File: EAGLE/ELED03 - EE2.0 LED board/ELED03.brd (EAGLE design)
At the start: 30 x 27.5 mm, 18 parts

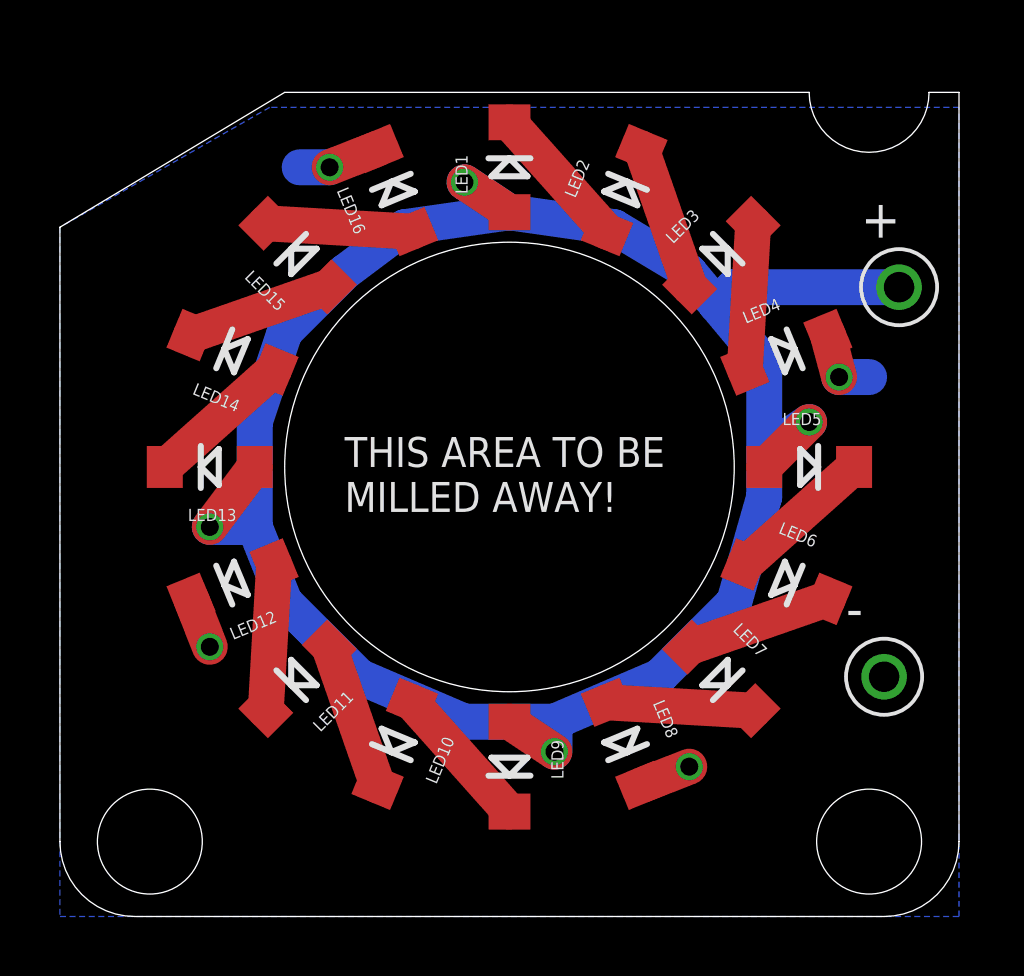
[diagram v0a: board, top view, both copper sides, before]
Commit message: On the two ring light boards, I changed the LEDs from 1206 package to 1210 in order to accomodate a brighter LED.
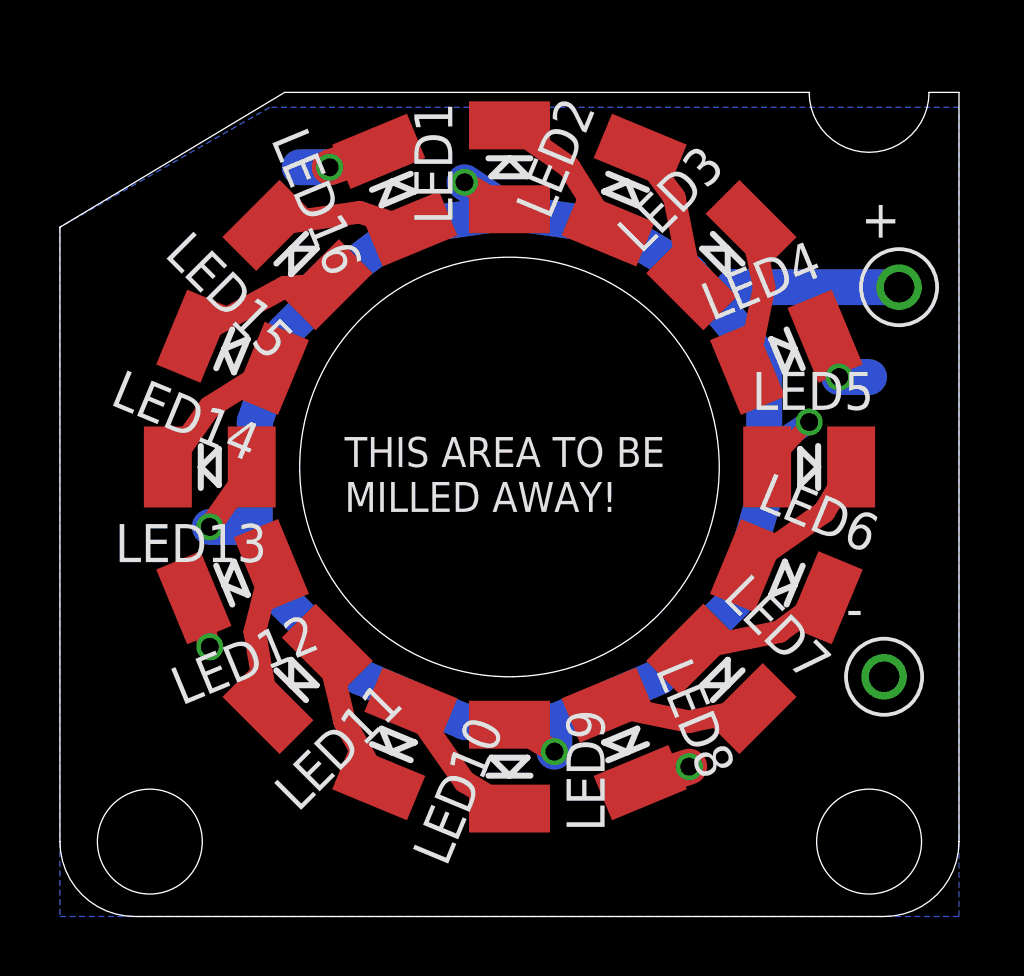
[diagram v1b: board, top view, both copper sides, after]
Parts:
- LED1, LED10, LED11, LED12, LED13, LED14, LED15, LED16, LED2, LED3, LED4, LED5, LED6, LED7, LED8, LED9: device SparkFun-LED:LED-1206-NO_SILK -> GinWhiskers - temp stuff:DIODE-1210
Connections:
- net -: now also LED12.K, LED16.K, LED4.K, LED8.K; no longer LED12.C, LED16.C, LED4.C, LED8.C
- net N$1: now also LED1.K; no longer LED1.C
- net N$10: now also LED15.K; no longer LED15.C
- net N$11: now also LED14.K; no longer LED14.C
- net N$12: now also LED13.K; no longer LED13.C
- net N$2: now also LED2.K; no longer LED2.C
- net N$3: now also LED3.K; no longer LED3.C
- net N$4: now also LED7.K; no longer LED7.C
- net N$5: now also LED6.K; no longer LED6.C
- net N$6: now also LED5.K; no longer LED5.C
- net N$7: now also LED9.K; no longer LED9.C
- net N$8: now also LED10.K; no longer LED10.C
- net N$9: now also LED11.K; no longer LED11.C
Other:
- outline, holes or cut-outs redrawn

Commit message: Added frames, logos, part numbers, and fiducials
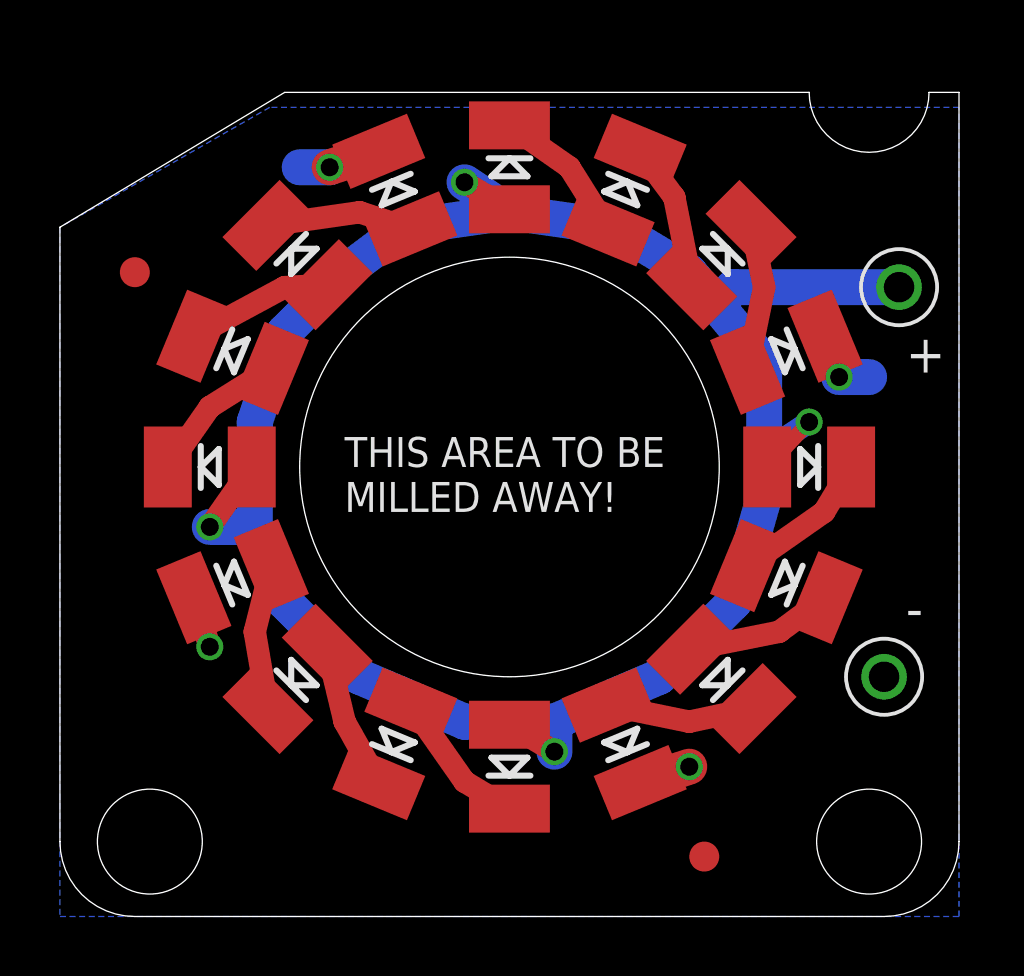
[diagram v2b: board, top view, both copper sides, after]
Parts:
- added FID1, FID2: FIDUCIAL, TinWhiskers:FIDUCIAL
- added LOGO4: LOGO-FIREPICKMEDIUM, FirePick:LOGO-FIREPICK-MEDIUM
- added U$1: TIN-WHISKERSSMALL, !tin-whiskers-logo:TIN-WHISKERS-SMALL
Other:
- board text added: "ELED03 Rev--"
